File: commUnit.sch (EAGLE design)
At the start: 13 parts

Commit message: dokreslen DPS
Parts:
- removed JP1, JP2: (no value), pinhead:PINHD-1X2
- removed JP3, JP4: (no value), pinhead:PINHD-1X6
- added NAP33: (no value), con-wago-508:W237-02P
- renumbered UART to UART1
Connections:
- removed net +5V: JP2.2, JP4.6
- removed net N$10: JP4.3, UART2-3.KL
- removed net N$3: JP3.3, U$1.URXD
- net +3V3: now also NAP33-2.KL; no longer JP1.1, JP3.1
- net GND: now also NAP33-1.KL; no longer JP1.2, JP2.1, JP3.2, JP4.5
- net N$5: now also U$1.URXD; no longer JP4.4
- net N$9: now also UART2-3.KL; no longer JP3.4
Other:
- moved on the sheet: UART2-3

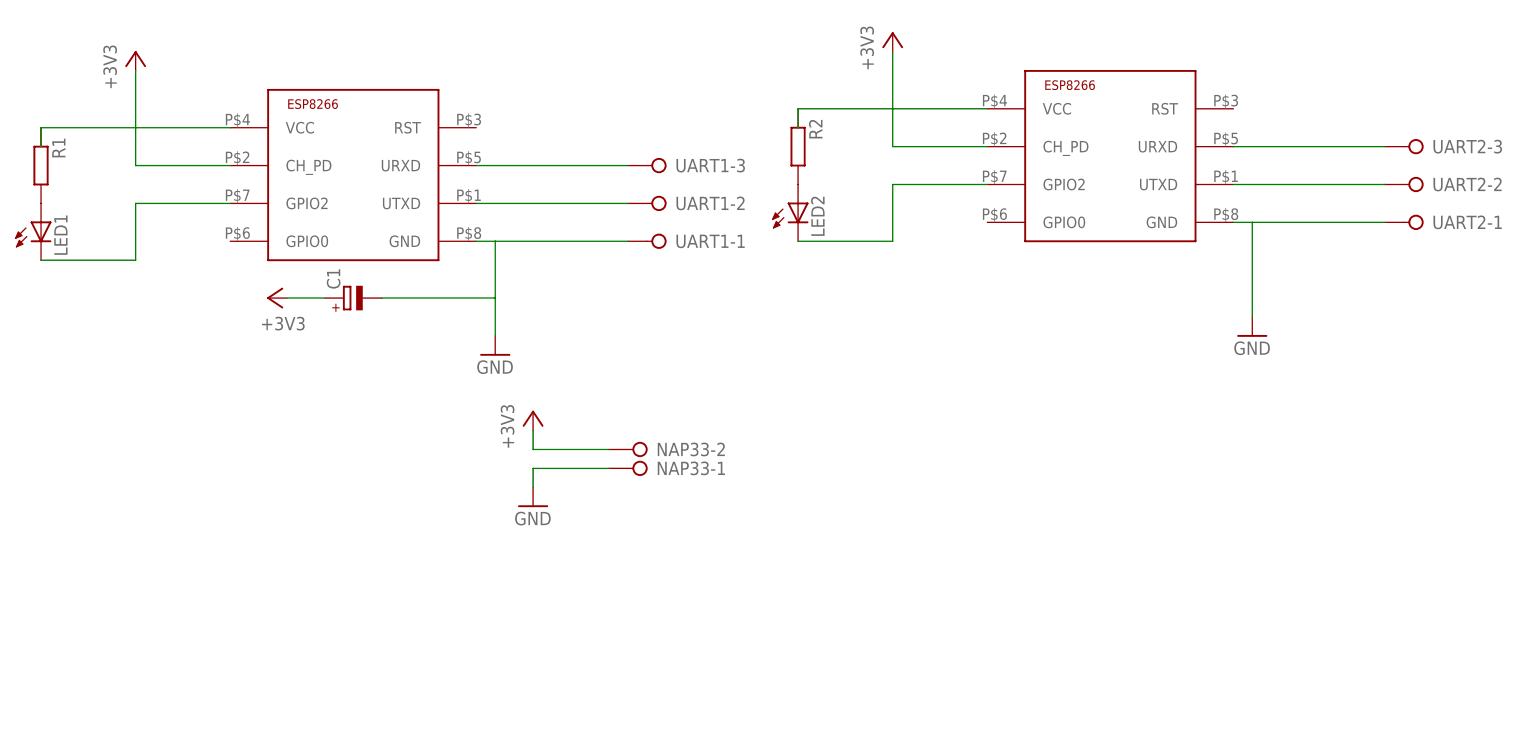
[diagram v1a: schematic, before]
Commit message: +upraveny DPS DPS objednany 27.4.2016
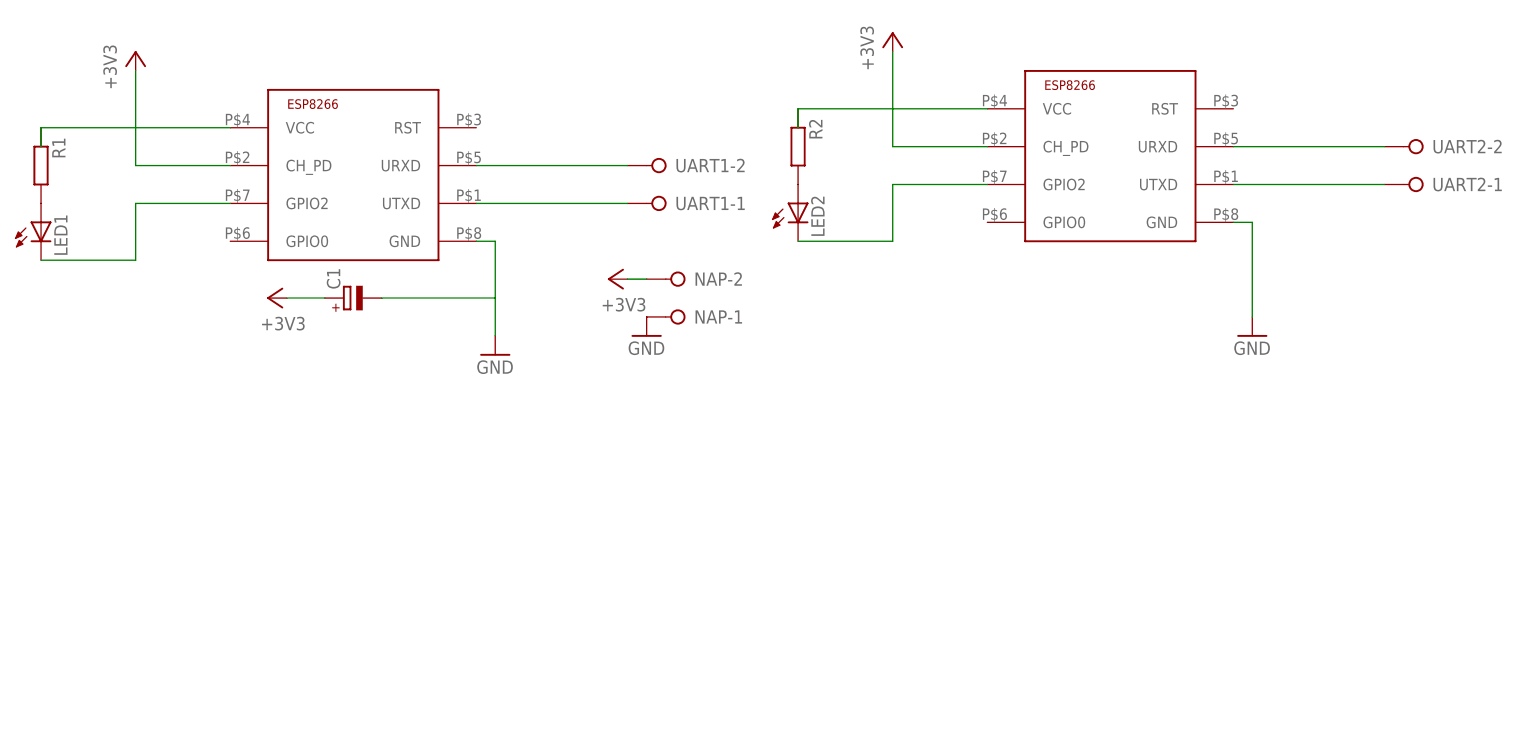
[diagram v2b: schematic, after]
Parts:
- removed NAP33: (no value), con-wago-508:W237-02P
- added NAP: (no value), con-wago-508:W237-02P
- UART1, UART2: device con-wago-508:W237-03P -> con-wago-508:W237-02P
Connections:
- removed net N$9: U$2.URXD, UART2-3.KL
- new net N$3: U$1.URXD, UART1-2.KL
- net +3V3: now also NAP-2.KL; no longer NAP33-2.KL
- net GND: now also NAP-1.KL; no longer NAP33-1.KL, UART1-1.KL, UART2-1.KL
- net N$4: now also UART1-1.KL; no longer UART1-2.KL
- net N$5: now also U$2.URXD, UART2-2.KL; no longer U$1.URXD, UART1-3.KL
- net N$8: now also UART2-1.KL; no longer UART2-2.KL
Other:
- moved on the sheet: UART1-1, UART1-2, UART2-1, UART2-2
